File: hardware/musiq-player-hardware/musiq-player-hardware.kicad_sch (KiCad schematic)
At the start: 60 parts, among them J1 Micro_SD_Card, J2 AudioJack3, J3 TP4056_CONN, J4 UART, SW1 SW_MEC_5E, SW2 SW_MEC_5E, SW3 SW_MEC_5E, SW4 SW_MEC_5E, SW5 SW_MEC_5E, SW6 RST, SW8 ON/OFF, U1 74LVC125, U2 W25Q128JVS, U4 AMS1117-3.3, U5 ESP32C3, U6 MAX98357AETE, Y2 40MHz

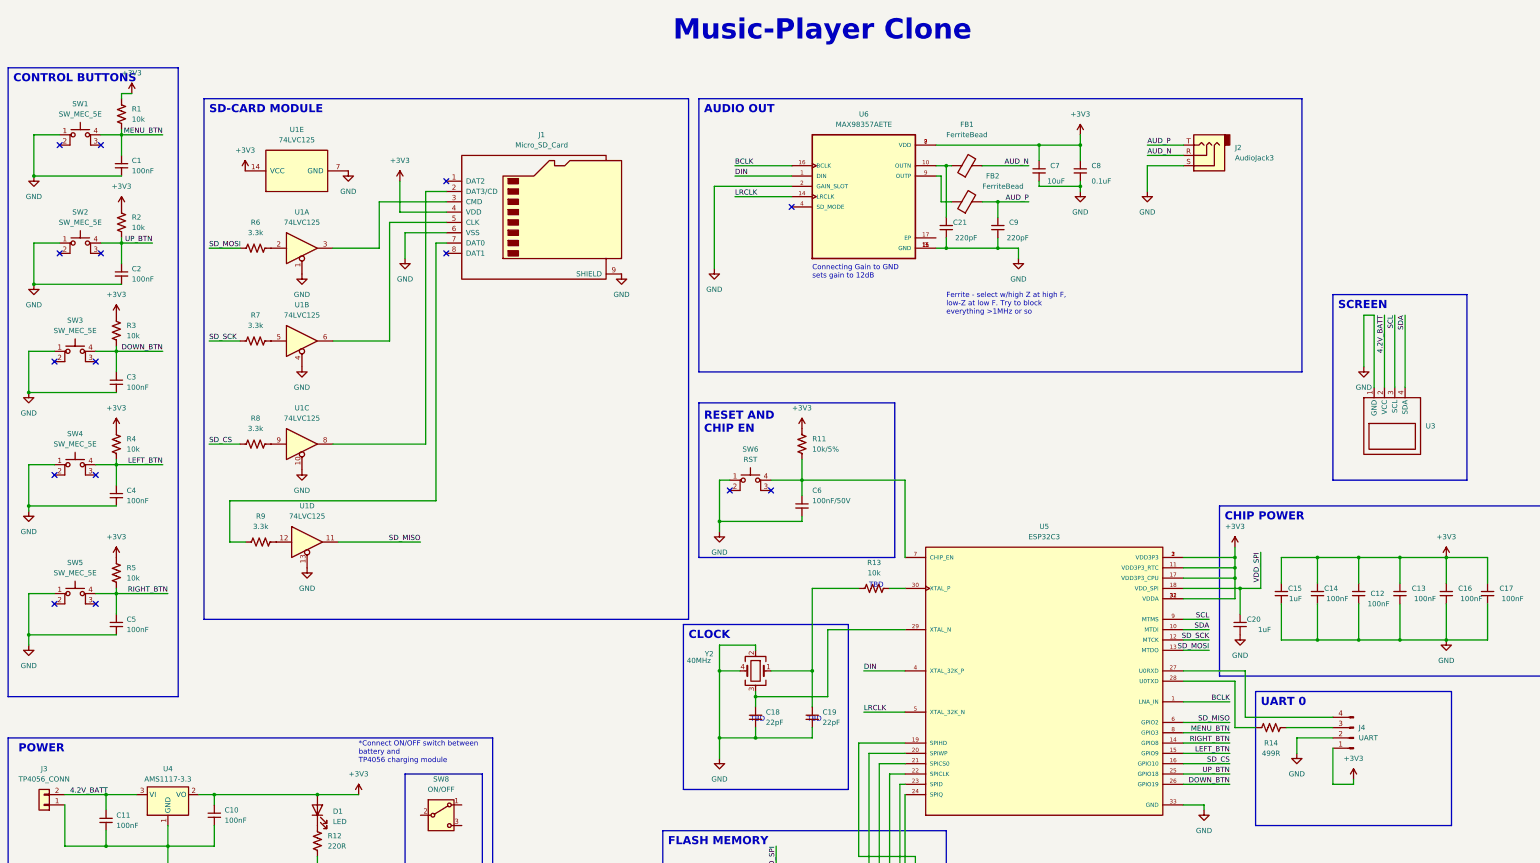
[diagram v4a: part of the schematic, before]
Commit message: adds complete PCB
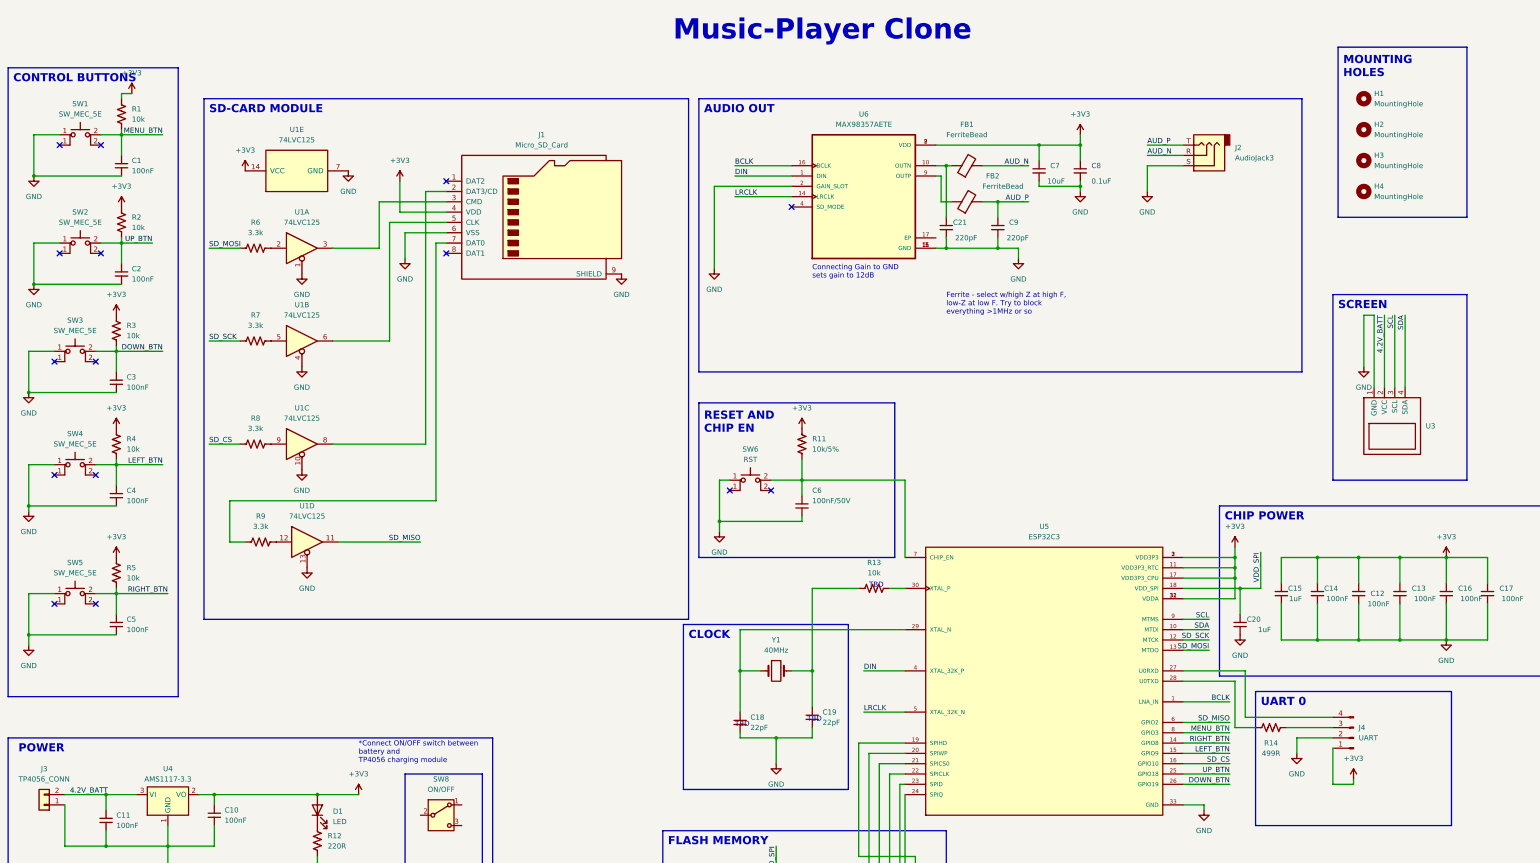
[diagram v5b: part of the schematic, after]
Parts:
- removed Y2: 40MHz, symbol Device:Crystal_GND23
- added H1, H2, H3, H4: MountingHole, MountingHole:MountingHole_2.2mm_M2, symbol Mechanical:MountingHole
- added Y1: 40MHz, Crystal:Crystal_HC49-U_Vertical, symbol Device:Crystal
- C1, C10, C11, C12, C13, C14, C15, C16, C17, C18, C19, C2, C20, C21, C3, C4, C5, C6, C7, C8, C9, FB1, FB2: footprint (none) -> Capacitor_SMD:C_0805_2012Metric_Pad1.18x1.45mm_HandSolder
- D1: footprint (none) -> LED_SMD:LED_0805_2012Metric_Pad1.15x1.40mm_HandSolder
- J1: footprint (none) -> custom-modules:SD-CARD-Adapter-alibaba
- J2: footprint (none) -> Connector_Audio:Jack_3.5mm_CUI_SJ1-3525N_Horizontal
- J3: footprint (none) -> Connector_PinHeader_2.54mm:PinHeader_1x02_P2.54mm_Vertical
- J4: footprint (none) -> Connector_PinHeader_2.54mm:PinHeader_1x04_P2.54mm_Vertical
- R1, R11, R12, R13, R14, R16, R17, R18, R19, R2, R20, R3, R4, R5, R6, R7, R8, R9: footprint (none) -> Resistor_SMD:R_0805_2012Metric_Pad1.20x1.40mm_HandSolder
- SW1, SW2, SW3, SW4, SW5: footprint (none) -> Button_Switch_SMD:SW_SPST_TL3342
- SW6: footprint (none) -> Button_Switch_SMD:SW_SPST_TL3305A
- SW8: footprint (none) -> Button_Switch_THT:SW_Push_1P2T_Vertical_E-Switch_800UDP8P1A1M6
- U1: footprint (none) -> Package_SO:TSSOP-14_4.4x5mm_P0.65mm
- U3: footprint (none) -> custom-modules:oled-ssd1306
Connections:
- net DOWN_BTN: now also SW3.2 (K); no longer SW3.4 (A)
- net LEFT_BTN: now also SW4.2 (K); no longer SW4.4 (A)
- net MENU_BTN: now also SW1.2 (K); no longer SW1.4 (A)
- net RIGHT_BTN: now also SW5.2 (K); no longer SW5.4 (A)
- net UP_BTN: now also SW2.2 (K); no longer SW2.4 (A)
- net at C19.1, R13.1: now also Y1.2
- net at C18.1, U5.29 (XTAL_N): now also Y1.1
- net at C6.1, R11.2, U5.7 (CHIP_EN): now also SW6.2 (K); no longer SW6.4 (A)
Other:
- note added: "MOUNTING HOLES"
- moved on the sheet: C18
